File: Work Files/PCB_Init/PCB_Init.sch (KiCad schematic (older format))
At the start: 35 parts

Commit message: Started designing PCB
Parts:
- removed J?: Micro_SD_Card, symbol Connector:Micro_SD_Card
- removed Roboclaw: Conn_01x03_Female, symbol Connector:Conn_01x03_Female
- BZ1: renamed from BZ?; footprint (none) -> Buzzer_Beeper:Buzzer_12x9.5RM7.6
- C1, C2, C3, C4, C5, C6: renamed from C?; value C -> 0.1u; footprint (none) -> Capacitor_THT:CP_Radial_D8.0mm_P5.00mm; Spice_Model (none) -> 0.1u; Spice_Netlist_Enabled (none) -> Y; Spice_Primitive (none) -> C
- C7: renamed from C?; value C -> 1u; footprint (none) -> Capacitor_THT:CP_Radial_D8.0mm_P5.00mm; Spice_Model (none) -> 1u; Spice_Netlist_Enabled (none) -> Y; Spice_Primitive (none) -> C
- J1, J3, J4, J5, J6, J7: renamed from J?; footprint (none) -> Connector_PinHeader_1.27mm:PinHeader_1x02_P1.27mm_Vertical
- J2: renamed from J?; footprint (none) -> TerminalBlock:TerminalBlock_Altech_AK300-2_P5.00mm
- LED1: renamed from D?; value LED -> 2V RED; footprint (none) -> LED_THT:LED_D3.0mm
- Pot1, Pot2, Pot3, Pot4: renamed from RV?; value R_POT_US -> 100k; footprint (none) -> Potentiometer_THT:Potentiometer_Bourns_3296W_Vertical; Spice_Model (none) -> 100k; Spice_Netlist_Enabled (none) -> Y; Spice_Primitive (none) -> R
- R1, R2: renamed from R?; value R_US -> 47k; footprint (none) -> Resistor_THT:R_Axial_DIN0204_L3.6mm_D1.6mm_P5.08mm_Horizontal; Spice_Model (none) -> 47k; Spice_Netlist_Enabled (none) -> Y; Spice_Primitive (none) -> R
- R3, R4, R5, R6: renamed from R?; value R_US -> 1k; footprint (none) -> Resistor_THT:R_Axial_DIN0204_L3.6mm_D1.6mm_P5.08mm_Horizontal; Spice_Model (none) -> 1k; Spice_Netlist_Enabled (none) -> Y; Spice_Primitive (none) -> R
- SW1, SW2, SW3, SW4: renamed from SW?; footprint (none) -> Button_Switch_THT:SW_PUSH-12mm
- U1: renamed from U?; footprint (none) -> Package_TO_SOT_THT:TO-3P-3_Vertical
- U3: renamed from U?; footprint (none) -> Sensor_Pressure:Honeywell_40PCxxxG1A
- gave numbers to parts that had none: 1
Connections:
- wire segments 23 -> 24
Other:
- moved on the sheet: C7, U3

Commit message: Started designing PCB2
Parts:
- J1, J3, J4, J5, J6, J7: footprint Connector_PinHeader_1.27mm:PinHeader_1x02_P1.27mm_Vertical -> Connector_PinHeader_2.54mm:PinHeader_1x02_P2.54mm_Vertical
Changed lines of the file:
@@
 F 0 "J3" H 1828 3876 50  0000 L CNN
 F 1 "Conn_01x02_Female" H 1828 3785 50  0000 L CNN
-F 2 "Connector_PinHeader_1.27mm:PinHeader_1x02_P1.27mm_Vertical" H 1800 3900 50  0001 C CNN
+F 2 "Connector_PinHeader_2.54mm:PinHeader_1x02_P2.54mm_Vertical" H 1800 3900 50  0001 C CNN
 F 3 "~" H 1800 3900 50  0001 C CNN
 	1    1800 3900
@@
 F 0 "J4" H 2478 3876 50  0000 L CNN
 F 1 "Conn_01x02_Female" H 2478 3785 50  0000 L CNN
-F 2 "Connector_PinHeader_1.27mm:PinHeader_1x02_P1.27mm_Vertical" H 2450 3900 50  0001 C CNN
+F 2 "Connector_PinHeader_2.54mm:PinHeader_1x02_P2.54mm_Vertical" H 2450 3900 50  0001 C CNN
 F 3 "~" H 2450 3900 50  0001 C CNN
 	1    2450 3900
@@
 F 0 "J5" H 3178 3876 50  0000 L CNN
 F 1 "Conn_01x02_Female" H 3178 3785 50  0000 L CNN
-F 2 "Connector_PinHeader_1.27mm:PinHeader_1x02_P1.27mm_Vertical" H 3150 3900 50  0001 C CNN
+F 2 "Connector_PinHeader_2.54mm:PinHeader_1x02_P2.54mm_Vertical" H 3150 3900 50  0001 C CNN
 F 3 "~" H 3150 3900 50  0001 C CNN
 	1    3150 3900
@@
 F 0 "J6" H 7528 2026 50  0000 L CNN
 F 1 "Conn_01x02_Female" H 7528 1935 50  0000 L CNN
-F 2 "Connector_PinHeader_1.27mm:PinHeader_1x02_P1.27mm_Vertical" H 7500 2050 50  0001 C CNN
+F 2 "Connector_PinHeader_2.54mm:PinHeader_1x02_P2.54mm_Vertical" H 7500 2050 50  0001 C CNN
 F 3 "~" H 7500 2050 50  0001 C CNN
 	1    7500 2050
@@
 F 0 "J1" H 1028 3876 50  0000 L CNN
 F 1 "Conn_01x02_Female" H 1028 3785 50  0000 L CNN
-F 2 "Connector_PinHeader_1.27mm:PinHeader_1x02_P1.27mm_Vertical" H 1000 3900 50  0001 C CNN
+F 2 "Connector_PinHeader_2.54mm:PinHeader_1x02_P2.54mm_Vertical" H 1000 3900 50  0001 C CNN
 F 3 "~" H 1000 3900 50  0001 C CNN
 	1    1000 3900
@@
 F 0 "J7" H 8828 2026 50  0000 L CNN
 F 1 "Conn_01x02_Female" H 8828 1935 50  0000 L CNN
-F 2 "Connector_PinHeader_1.27mm:PinHeader_1x02_P1.27mm_Vertical" H 8800 2050 50  0001 C CNN
+F 2 "Connector_PinHeader_2.54mm:PinHeader_1x02_P2.54mm_Vertical" H 8800 2050 50  0001 C CNN
 F 3 "~" H 8800 2050 50  0001 C CNN
 	1    8800 2050

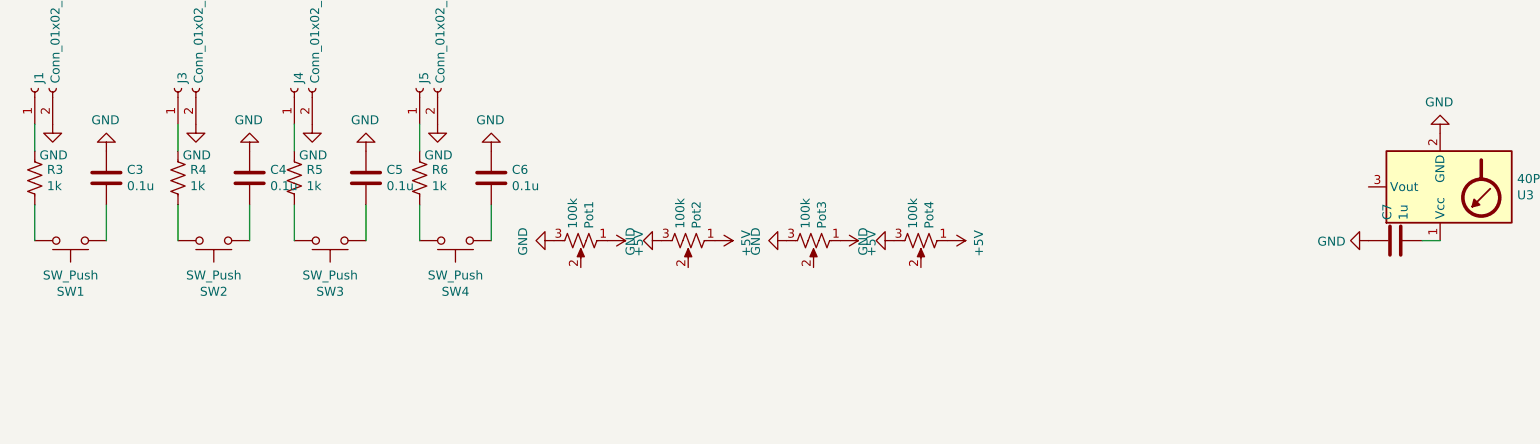
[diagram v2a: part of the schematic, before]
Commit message: Started designing ing PCB 4
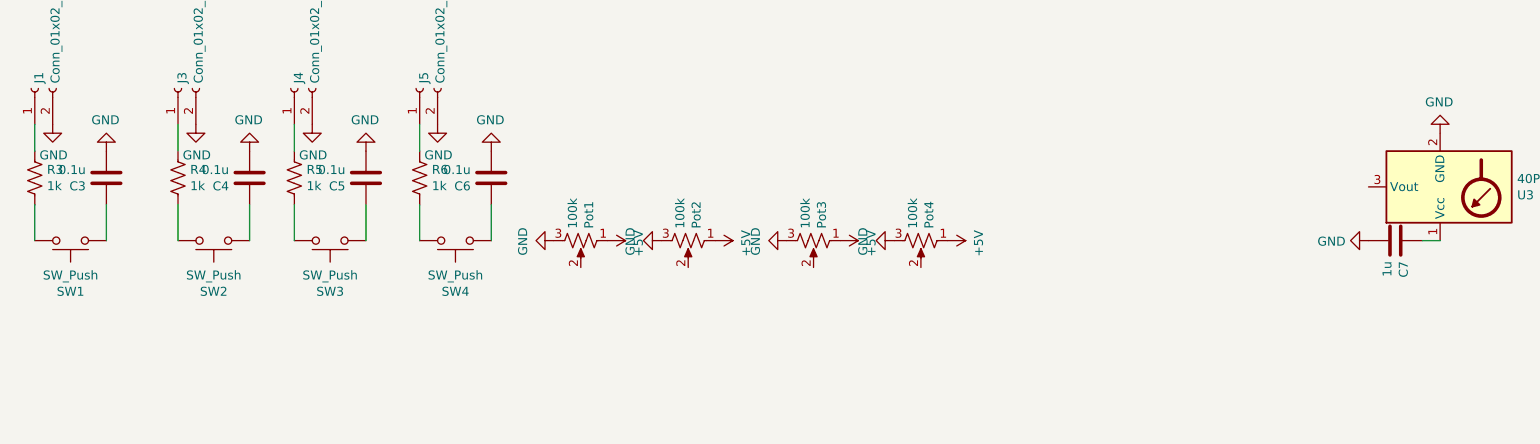
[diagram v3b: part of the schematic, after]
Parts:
- SW1, SW2, SW3, SW4: footprint Button_Switch_THT:SW_PUSH-12mm -> Button_Switch_THT:SW_CW_GPTS203211B
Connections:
- net GND: now also C3.2, C4.2, C5.2, C6.2, C7.2; no longer C3.1, C4.1, C5.1, C6.1, C7.1
- net at U3.1 (Vcc): now also C7.1; no longer C7.2
- net at SW1.1: now also C3.1; no longer C3.2
- net at SW2.1: now also C4.1; no longer C4.2
- net at SW4.1: now also C6.1; no longer C6.2
- net at SW3.1: now also C5.1; no longer C5.2
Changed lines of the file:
@@
 F 6 "Y" H 1400 4400 50  0001 C CNN "Spice_Netlist_Enabled"
 	1    1400 4400
-	1    0    0    -1
+	-1   0    0    1
 $EndComp
 $Comp
@@
 F 6 "Y" H 2200 4400 50  0001 C CNN "Spice_Netlist_Enabled"
 	1    2200 4400
-	1    0    0    -1
+	-1   0    0    1
 $EndComp
 $Comp
@@
 F 6 "Y" H 3550 4400 50  0001 C CNN "Spice_Netlist_Enabled"
 	1    3550 4400
-	1    0    0    -1
+	-1   0    0    1
 $EndComp
 $Comp
@@
 F 6 "Y" H 2850 4400 50  0001 C CNN "Spice_Netlist_Enabled"
 	1    2850 4400
-	1    0    0    -1
+	-1   0    0    1
 $EndComp
 $Comp
@@
 F 6 "Y" H 8600 4750 50  0001 C CNN "Spice_Netlist_Enabled"
 	1    8600 4750
-	0    -1   -1   0
+	0    1    1    0
 $EndComp
 $Comp
@@
 F 0 "SW2" H 2000 5035 50  0000 C CNN
 F 1 "SW_Push" H 2000 4944 50  0000 C CNN
-F 2 "Button_Switch_THT:SW_PUSH-12mm" H 2000 4950 50  0001 C CNN
+F 2 "Button_Switch_THT:SW_CW_GPTS203211B" H 2000 4950 50  0001 C CNN
 F 3 "~" H 2000 4950 50  0001 C CNN
 	1    2000 4750
@@
 F 0 "SW4" H 3350 5035 50  0000 C CNN
 F 1 "SW_Push" H 3350 4944 50  0000 C CNN
-F 2 "Button_Switch_THT:SW_PUSH-12mm" H 3350 4950 50  0001 C CNN
+F 2 "Button_Switch_THT:SW_CW_GPTS203211B" H 3350 4950 50  0001 C CNN
 F 3 "~" H 3350 4950 50  0001 C CNN
 	1    3350 4750
@@
 F 0 "SW3" H 2650 5035 50  0000 C CNN
 F 1 "SW_Push" H 2650 4944 50  0000 C CNN
-F 2 "Button_Switch_THT:SW_PUSH-12mm" H 2650 4950 50  0001 C CNN
+F 2 "Button_Switch_THT:SW_CW_GPTS203211B" H 2650 4950 50  0001 C CNN
 F 3 "~" H 2650 4950 50  0001 C CNN
 	1    2650 4750
@@
 F 0 "SW1" H 1200 5035 50  0000 C CNN
 F 1 "SW_Push" H 1200 4944 50  0000 C CNN
-F 2 "Button_Switch_THT:SW_PUSH-12mm" H 1200 4950 50  0001 C CNN
+F 2 "Button_Switch_THT:SW_CW_GPTS203211B" H 1200 4950 50  0001 C CNN
 F 3 "~" H 1200 4950 50  0001 C CNN
 	1    1200 4750

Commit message: Plotted gerber files for initial idea3
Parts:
- added R7: 4.7k, Resistor_THT:R_Axial_DIN0204_L3.6mm_D1.6mm_P5.08mm_Horizontal, symbol Device:R_US
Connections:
- net +5V: now also R7.1
- net at U2.16 (K): now also R7.2
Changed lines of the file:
@@
 Wire Wire Line
 	3150 4550 3150 4750
+$Comp
+L Device:R_US R7
+U 1 1 607FE3A9
+P 5350 900
+F 0 "R7" H 5418 946 50  0000 L CNN
+F 1 "4.7k" H 5418 855 50  0000 L CNN
+F 2 "Resistor_THT:R_Axial_DIN0204_L3.6mm_D1.6mm_P5.08mm_Horizontal" V 5390 890 50  0001 C CNN
+F 3 "~" H 5350 900 50  0001 C CNN
+F 4 "R" H 5350 900 50  0001 C CNN "Spice_Primitive"
+F 5 "4.7k" H 5350 900 50  0001 C CNN "Spice_Model"
+F 6 "Y" H 5350 900 50  0001 C CNN "Spice_Netlist_Enabled"
+	1    5350 900
+	1    0    0    -1
+$EndComp
+$Comp
+L power:+5V #PWR034
+U 1 1 607FEDA5
+P 5350 750
+F 0 "#PWR034" H 5350 600 50  0001 C CNN
+F 1 "+5V" H 5365 923 50  0000 C CNN
+F 2 "" H 5350 750 50  0001 C CNN
+F 3 "" H 5350 750 50  0001 C CNN
+	1    5350 750
+	1    0    0    -1
+$EndComp
 $EndSCHEMATC

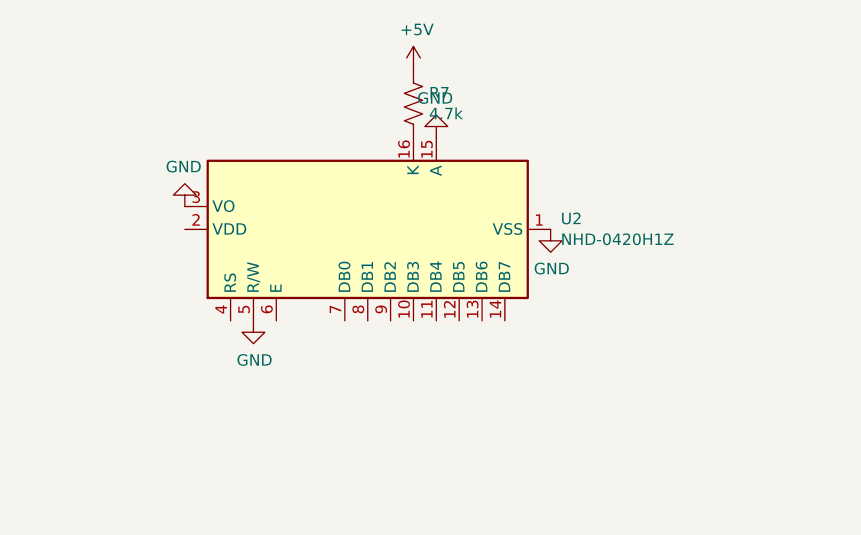
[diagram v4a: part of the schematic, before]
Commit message: PCB update with LCD 16x2
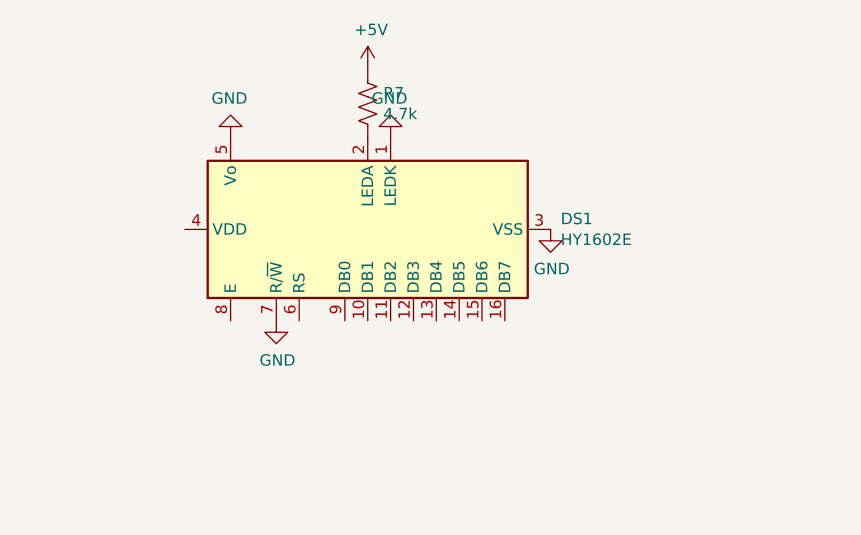
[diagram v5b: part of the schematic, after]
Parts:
- removed U2: NHD-0420H1Z, Display:NHD-0420H1Z, symbol Display_Character:NHD-0420H1Z
- added DS1: HY1602E, Display:HY1602E, symbol Display_Character:HY1602E
- R1, R2, R3, R4, R5, R6, R7: footprint Resistor_THT:R_Axial_DIN0204_L3.6mm_D1.6mm_P5.08mm_Horizontal -> Resistor_THT:R_Axial_DIN0207_L6.3mm_D2.5mm_P10.16mm_Horizontal
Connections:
- net GND: now also DS1.1 (LEDK), DS1.3 (VSS), DS1.5 (Vo), DS1.7 (R/~W)
- net at R7.2: now also DS1.2 (LEDA)
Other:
- moved on the sheet: R7
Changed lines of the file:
@@
-$EndComp
-$Comp
-L Display_Character:NHD-0420H1Z U2
-U 1 1 605F2D85
-P 5150 1450
-F 0 "U2" V 5196 606 50  0000 R CNN
-F 1 "NHD-0420H1Z" V 5105 606 50  0000 R CNN
-F 2 "Display:NHD-0420H1Z" H 5150 550 50  0001 C CNN
-F 3 "http://www.newhavendisplay.com/specs/NHD-0420H1Z-FSW-GBW-33V3.pdf" H 5250 1350 50  0001 C CNN
-	1    5150 1450
-	0    -1   -1   0
 $EndComp
 $Comp
@@
 F 0 "R1" H 7568 1596 50  0000 L CNN
 F 1 "47k" H 7568 1505 50  0000 L CNN
-F 2 "Resistor_THT:R_Axial_DIN0204_L3.6mm_D1.6mm_P5.08mm_Horizontal" V 7540 1540 50  0001 C CNN
+F 2 "Resistor_THT:R_Axial_DIN0207_L6.3mm_D2.5mm_P10.16mm_Horizontal" V 7540 1540 50  0001 C CNN
 F 3 "~" H 7500 1550 50  0001 C CNN
 F 4 "R" H 7500 1550 50  0001 C CNN "Spice_Primitive"
@@
 F 0 "R4" H 1868 4446 50  0000 L CNN
 F 1 "1k" H 1868 4355 50  0000 L CNN
-F 2 "Resistor_THT:R_Axial_DIN0204_L3.6mm_D1.6mm_P5.08mm_Horizontal" V 1840 4390 50  0001 C CNN
+F 2 "Resistor_THT:R_Axial_DIN0207_L6.3mm_D2.5mm_P10.16mm_Horizontal" V 1840 4390 50  0001 C CNN
 F 3 "~" H 1800 4400 50  0001 C CNN
 F 4 "R" H 1800 4400 50  0001 C CNN "Spice_Primitive"
@@
 F 0 "R3" H 1068 4446 50  0000 L CNN
 F 1 "1k" H 1068 4355 50  0000 L CNN
-F 2 "Resistor_THT:R_Axial_DIN0204_L3.6mm_D1.6mm_P5.08mm_Horizontal" V 1040 4390 50  0001 C CNN
+F 2 "Resistor_THT:R_Axial_DIN0207_L6.3mm_D2.5mm_P10.16mm_Horizontal" V 1040 4390 50  0001 C CNN
 F 3 "~" H 1000 4400 50  0001 C CNN
 F 4 "R" H 1000 4400 50  0001 C CNN "Spice_Primitive"
@@
 F 0 "R2" H 8868 1596 50  0000 L CNN
 F 1 "47k" H 8868 1505 50  0000 L CNN
-F 2 "Resistor_THT:R_Axial_DIN0204_L3.6mm_D1.6mm_P5.08mm_Horizontal" V 8840 1540 50  0001 C CNN
+F 2 "Resistor_THT:R_Axial_DIN0207_L6.3mm_D2.5mm_P10.16mm_Horizontal" V 8840 1540 50  0001 C CNN
 F 3 "~" H 8800 1550 50  0001 C CNN
 F 4 "R" H 8800 1550 50  0001 C CNN "Spice_Primitive"
@@
 F 0 "R6" H 3218 4446 50  0000 L CNN
 F 1 "1k" H 3218 4355 50  0000 L CNN
-F 2 "Resistor_THT:R_Axial_DIN0204_L3.6mm_D1.6mm_P5.08mm_Horizontal" V 3190 4390 50  0001 C CNN
+F 2 "Resistor_THT:R_Axial_DIN0207_L6.3mm_D2.5mm_P10.16mm_Horizontal" V 3190 4390 50  0001 C CNN
 F 3 "~" H 3150 4400 50  0001 C CNN
 F 4 "R" H 3150 4400 50  0001 C CNN "Spice_Primitive"
@@
 F 0 "R5" H 2518 4446 50  0000 L CNN
 F 1 "1k" H 2518 4355 50  0000 L CNN
-F 2 "Resistor_THT:R_Axial_DIN0204_L3.6mm_D1.6mm_P5.08mm_Horizontal" V 2490 4390 50  0001 C CNN
+F 2 "Resistor_THT:R_Axial_DIN0207_L6.3mm_D2.5mm_P10.16mm_Horizontal" V 2490 4390 50  0001 C CNN
 F 3 "~" H 2450 4400 50  0001 C CNN
 F 4 "R" H 2450 4400 50  0001 C CNN "Spice_Primitive"
@@
 L power:GND #PWR020
 U 1 1 607158CF
-P 4650 1850
-F 0 "#PWR020" H 4650 1600 50  0001 C CNN
-F 1 "GND" H 4655 1677 50  0000 C CNN
-F 2 "" H 4650 1850 50  0001 C CNN
-F 3 "" H 4650 1850 50  0001 C CNN
-	1    4650 1850
+P 4750 1850
+F 0 "#PWR020" H 4750 1600 50  0001 C CNN
+F 1 "GND" H 4755 1677 50  0000 C CNN
+F 2 "" H 4750 1850 50  0001 C CNN
+F 3 "" H 4750 1850 50  0001 C CNN
+	1    4750 1850
 	1    0    0    -1
 $EndComp
@@
 L power:GND #PWR018
 U 1 1 6071858A
-P 4350 1350
-F 0 "#PWR018" H 4350 1100 50  0001 C CNN
-F 1 "GND" H 4355 1177 50  0000 C CNN
-F 2 "" H 4350 1350 50  0001 C CNN
-F 3 "" H 4350 1350 50  0001 C CNN
-	1    4350 1350
+P 4550 1050
+F 0 "#PWR018" H 4550 800 50  0001 C CNN
+F 1 "GND" H 4555 877 50  0000 C CNN
+F 2 "" H 4550 1050 50  0001 C CNN
+F 3 "" H 4550 1050 50  0001 C CNN
+	1    4550 1050
 	-1   0    0    1
 $EndComp
@@
 L power:GND #PWR023
 U 1 1 60718DAB
-P 5450 1050
-F 0 "#PWR023" H 5450 800 50  0001 C CNN
-F 1 "GND" H 5455 877 50  0000 C CNN
-F 2 "" H 5450 1050 50  0001 C CNN
-F 3 "" H 5450 1050 50  0001 C CNN
-	1    5450 1050
+P 5250 1050
+F 0 "#PWR023" H 5250 800 50  0001 C CNN
+F 1 "GND" H 5255 877 50  0000 C CNN
+F 2 "" H 5250 1050 50  0001 C CNN
+F 3 "" H 5250 1050 50  0001 C CNN
+	1    5250 1050
 	-1   0    0    1
 $EndComp
@@
 L Device:R_US R7
 U 1 1 607FE3A9
-P 5350 900
-F 0 "R7" H 5418 946 50  0000 L CNN
-F 1 "4.7k" H 5418 855 50  0000 L CNN
-F 2 "Resistor_THT:R_Axial_DIN0204_L3.6mm_D1.6mm_P5.08mm_Horizontal" V 5390 890 50  0001 C CNN
-F 3 "~" H 5350 900 50  0001 C CNN
-F 4 "R" H 5350 900 50  0001 C CNN "Spice_Primitive"
-F 5 "4.7k" H 5350 900 50  0001 C CNN "Spice_Model"
-F 6 "Y" H 5350 900 50  0001 C CNN "Spice_Netlist_Enabled"
-	1    5350 900
+P 5150 900
+F 0 "R7" H 5218 946 50  0000 L CNN
+F 1 "4.7k" H 5218 855 50  0000 L CNN
+F 2 "Resistor_THT:R_Axial_DIN0207_L6.3mm_D2.5mm_P10.16mm_Horizontal" V 5190 890 50  0001 C CNN
+F 3 "~" H 5150 900 50  0001 C CNN
+F 4 "R" H 5150 900 50  0001 C CNN "Spice_Primitive"
+F 5 "4.7k" H 5150 900 50  0001 C CNN "Spice_Model"
+F 6 "Y" H 5150 900 50  0001 C CNN "Spice_Netlist_Enabled"
+	1    5150 900
 	1    0    0    -1
 $EndComp
@@
 L power:+5V #PWR034
 U 1 1 607FEDA5
-P 5350 750
-F 0 "#PWR034" H 5350 600 50  0001 C CNN
-F 1 "+5V" H 5365 923 50  0000 C CNN
-F 2 "" H 5350 750 50  0001 C CNN
-F 3 "" H 5350 750 50  0001 C CNN
-	1    5350 750
-	1    0    0    -1
+P 5150 750
+F 0 "#PWR034" H 5150 600 50  0001 C CNN
+F 1 "+5V" H 5165 923 50  0000 C CNN
+F 2 "" H 5150 750 50  0001 C CNN
+F 3 "" H 5150 750 50  0001 C CNN
+	1    5150 750
+	1    0    0    -1
+$EndComp
+$Comp
+L Display_Character:HY1602E DS1
+U 1 1 6080687F
+P 5150 1450
+F 0 "DS1" V 5196 606 50  0000 R CNN
+F 1 "HY1602E" V 5105 606 50  0000 R CNN
+F 2 "Display:HY1602E" H 5150 550 50  0001 C CIN
+F 3 "http://www.icbank.com/data/ICBShop/board/HY1602E.pdf" H 5350 1550 50  0001 C CNN
+	1    5150 1450
+	0    -1   -1   0
 $EndComp
 $EndSCHEMATC
